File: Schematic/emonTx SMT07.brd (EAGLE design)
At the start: 100 x 80.3 mm, 115 parts, among them IC1 4066D, IC2 4066D, IC3 LMV324, J1 CON_HEADER_PRG_AVR_ICSP, Q2 DS18B20, U2 ATMEGA32U4, X10 BU-SMA-H, X2 CT2, X3 CT3, X4 STEREOJACK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

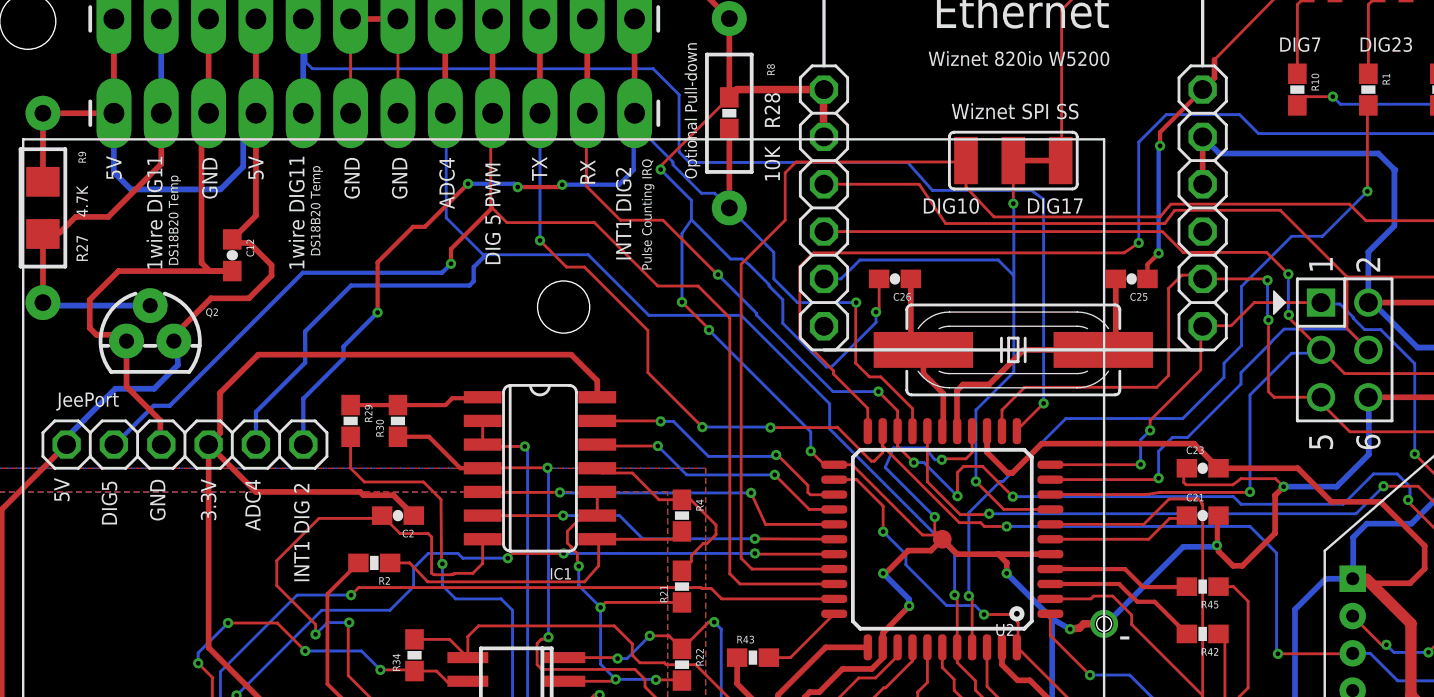
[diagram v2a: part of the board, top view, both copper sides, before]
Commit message: connect wiznet reset to dig5, need to route
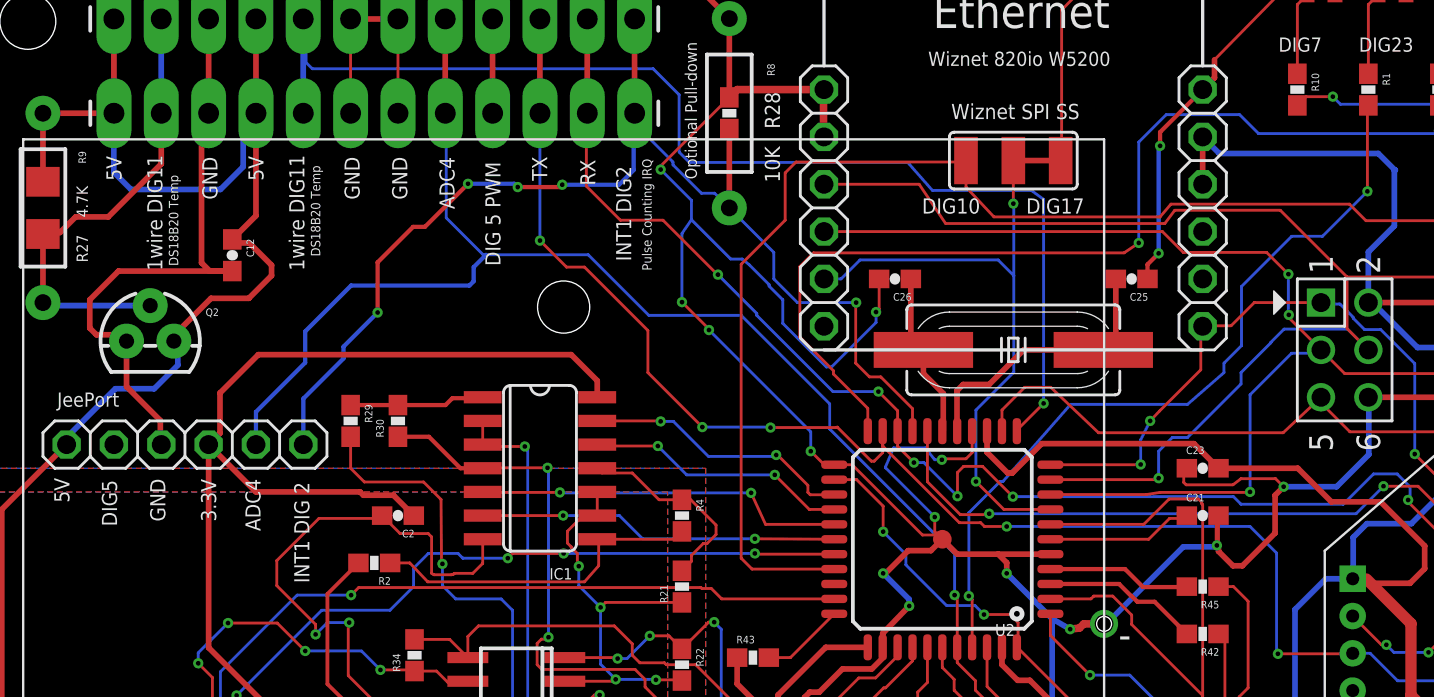
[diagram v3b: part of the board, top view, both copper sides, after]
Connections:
- net DIG5: now also JP3.5
- net RST: no longer JP3.5
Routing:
- net DIG5: track 71.0 -> 5.06 mm, vias 1 -> 0
- net RST: track 85.0 -> 75.3 mm, vias 2 -> 0
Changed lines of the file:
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@@
 <setting verticaltext="up"/>
 </settings>
-<grid distance="50" unitdist="mil" unit="mil" style="lines" multiple="1" display="yes" altdistance="50" altunitdist="mil" altunit="mil"/>
+<grid distance="5" unitdist="mil" unit="mil" style="lines" multiple="1" display="yes" altdistance="50" altunitdist="mil" altunit="mil"/>
 <layers>
 <layer number="1" name="Top" color="4" fill="1" visible="yes" active="yes"/>
@@
 <wire x1="55.27" y1="55.33" x2="55.27" y2="56.4638" width="0.1524" layer="1"/>
 <wire x1="55.27" y1="56.4638" x2="56.4896" y2="57.6834" width="0.1524" layer="1"/>
-<wire x1="56.4896" y1="57.6834" x2="63.5762" y2="57.6834" width="0.1524" layer="1"/>
-<wire x1="63.5762" y1="57.6834" x2="64.2112" y2="58.3184" width="0.1524" layer="1"/>
-<wire x1="64.2112" y1="58.3184" x2="64.2112" y2="62.992" width="0.1524" layer="1"/>
-<via x="69.5198" y="63.4238" extent="1-16" drill="0.25"/>
-<wire x1="69.5198" y1="63.4238" x2="69.5198" y2="61.341" width="0.1524" layer="16"/>
-<wire x1="69.5198" y1="61.341" x2="69.5706" y2="61.2902" width="0.1524" layer="16"/>
-<via x="69.5706" y="61.2902" extent="1-16" drill="0.25"/>
-<wire x1="69.5706" y1="61.2902" x2="69.5706" y2="57.4548" width="0.1524" layer="1"/>
-<wire x1="69.5706" y1="57.4548" x2="69.8754" y2="57.15" width="0.1524" layer="1"/>
-<wire x1="69.8754" y1="57.15" x2="72.39" y2="57.15" width="0.1524" layer="1"/>
 <wire x1="72.39" y1="57.15" x2="72.39" y2="56.8452" width="0.1524" layer="1"/>
 <wire x1="72.39" y1="56.8452" x2="73.9394" y2="55.2958" width="0.1524" layer="1"/>
@@
 <wire x1="97.116" y1="26.924" x2="97.4852" y2="26.924" width="0.1524" layer="1"/>
 <wire x1="97.4852" y1="26.924" x2="99.2886" y2="28.7274" width="0.1524" layer="1"/>
-<contactref element="JP3" pad="5"/>
-<wire x1="64.2112" y1="62.992" x2="64.9224" y2="63.7032" width="0.1524" layer="1"/>
-<wire x1="64.9224" y1="63.7032" x2="65.8368" y2="63.7032" width="0.1524" layer="1"/>
-<wire x1="65.8368" y1="63.7032" x2="66.04" y2="63.5" width="0.1524" layer="1"/>
-<wire x1="66.04" y1="63.5" x2="69.4436" y2="63.5" width="0.1524" layer="1"/>
-<wire x1="69.4436" y1="63.5" x2="69.5198" y2="63.4238" width="0.1524" layer="1"/>
+<wire x1="56.4896" y1="57.6834" x2="57.8866" y2="57.6834" width="0.1524" layer="1"/>
+<wire x1="57.8866" y1="57.6834" x2="60.452" y2="55.245" width="0.1524" layer="1"/>
+<wire x1="60.452" y1="55.245" x2="70.358" y2="55.245" width="0.1524" layer="1"/>
+<wire x1="70.358" y1="55.245" x2="72.39" y2="57.15" width="0.1524" layer="1"/>
 <wire x1="91.44" y1="7.112" x2="97.116" y2="26.924" width="0" layer="19" extent="1-1"/>
 </signal>
@@
 <via x="62.7126" y="53.5432" extent="1-16" drill="0.25"/>
 <wire x1="62.7126" y1="53.5432" x2="62.7126" y2="54.864" width="0.1524" layer="16"/>
-<wire x1="62.7126" y1="54.864" x2="63.2206" y2="55.372" width="0.1524" layer="16"/>
-<via x="63.2206" y="55.372" extent="1-16" drill="0.25"/>
-<wire x1="63.2206" y1="55.372" x2="63.2206" y2="55.9054" width="0.1524" layer="1"/>
-<wire x1="63.2206" y1="55.9054" x2="65.9384" y2="58.6232" width="0.1524" layer="1"/>
+<wire x1="62.7126" y1="54.864" x2="63.2206" y2="55.88" width="0.1524" layer="16"/>
+<via x="63.2206" y="55.88" extent="1-16" drill="0.25"/>
+<wire x1="63.2206" y1="55.88" x2="63.7286" y2="56.4134" width="0.1524" layer="1"/>
+<wire x1="63.7286" y1="56.4134" x2="65.9384" y2="58.6232" width="0.1524" layer="1"/>
 <wire x1="65.9384" y1="58.6232" x2="65.9384" y2="60.8584" width="0.1524" layer="1"/>
 <wire x1="65.9384" y1="60.8584" x2="66.04" y2="60.96" width="0.1524" layer="1"/>
@@
 <wire x1="53.4924" y1="50.9524" x2="55.1688" y2="52.6288" width="0.1524" layer="16"/>
 <wire x1="55.1688" y1="52.6288" x2="55.3212" y2="52.6288" width="0.1524" layer="16"/>
-<wire x1="55.3212" y1="52.6288" x2="58.6994" y2="56.007" width="0.1524" layer="16"/>
-<wire x1="58.6994" y1="56.007" x2="64.9732" y2="56.007" width="0.1524" layer="16"/>
-<wire x1="64.9732" y1="56.007" x2="67.183" y2="58.2168" width="0.1524" layer="16"/>
-<wire x1="67.183" y1="58.2168" x2="67.183" y2="58.9788" width="0.1524" layer="16"/>
+<wire x1="55.3212" y1="52.6288" x2="58.9534" y2="56.769" width="0.1524" layer="16"/>
+<wire x1="58.9534" y1="56.769" x2="65.2272" y2="56.769" width="0.1524" layer="16"/>
+<wire x1="65.2272" y1="56.769" x2="67.183" y2="58.4708" width="0.1524" layer="16"/>
+<wire x1="67.183" y1="58.4708" x2="67.183" y2="58.9788" width="0.1524" layer="16"/>
 <wire x1="67.183" y1="58.9788" x2="68.1228" y2="59.9186" width="0.1524" layer="16"/>
 <wire x1="68.1228" y1="59.9186" x2="68.1228" y2="63.0936" width="0.1524" layer="16"/>
@@
 <contactref element="JP5" pad="9"/>
 <contactref element="JP6" pad="2"/>
-<wire x1="46.27" y1="47.13" x2="41.2112" y2="47.13" width="0.1524" layer="1"/>
-<wire x1="41.2112" y1="47.13" x2="40.6654" y2="47.6758" width="0.1524" layer="1"/>
-<wire x1="40.6654" y1="47.6758" x2="40.6654" y2="61.4172" width="0.1524" layer="1"/>
-<wire x1="40.6654" y1="61.4172" x2="38.9636" y2="63.119" width="0.1524" layer="1"/>
-<wire x1="38.9636" y1="63.119" x2="36.8046" y2="63.119" width="0.1524" layer="1"/>
-<wire x1="36.8046" y1="63.119" x2="33.401" y2="66.5226" width="0.1524" layer="1"/>
-<wire x1="33.401" y1="66.5226" x2="28.702" y2="66.5226" width="0.1524" layer="1"/>
-<wire x1="28.702" y1="66.5226" x2="27.9146" y2="67.31" width="0.1524" layer="1"/>
-<wire x1="27.9146" y1="67.31" x2="27.8384" y2="67.3862" width="0.1524" layer="1"/>
-<wire x1="27.8384" y1="67.3862" x2="27.8384" y2="72.2884" width="0.1524" layer="1"/>
-<wire x1="27.8384" y1="72.2884" x2="27.94" y2="72.39" width="0.1524" layer="1"/>
-<wire x1="7.62" y1="54.61" x2="7.6708" y2="54.61" width="0.2286" layer="16"/>
-<wire x1="7.6708" y1="54.61" x2="9.7536" y2="56.6928" width="0.2286" layer="16"/>
-<wire x1="9.7536" y1="56.6928" x2="10.6172" y2="56.6928" width="0.2286" layer="16"/>
-<wire x1="10.6172" y1="56.6928" x2="17.7546" y2="63.8302" width="0.2286" layer="16"/>
-<wire x1="17.7546" y1="63.8302" x2="25.2222" y2="63.8302" width="0.2286" layer="16"/>
-<wire x1="25.2222" y1="63.8302" x2="25.7048" y2="64.3128" width="0.2286" layer="16"/>
-<via x="25.7048" y="64.3128" extent="1-16" drill="0.25"/>
-<wire x1="25.7048" y1="64.3128" x2="25.7048" y2="65.1002" width="0.2286" layer="1"/>
-<wire x1="25.7048" y1="65.1002" x2="27.9146" y2="67.31" width="0.2286" layer="1"/>
 <wire x1="27.9364375" y1="77.45100625" x2="27.9364375" y2="72.3935625" width="0.3048" layer="1"/>
 <wire x1="27.9364375" y1="72.3935625" x2="27.94" y2="72.39" width="0.3048" layer="1"/>
+<contactref element="JP3" pad="5"/>
+<wire x1="46.27" y1="47.13" x2="66.04" y2="63.5" width="0" layer="19" extent="1-1"/>
+<wire x1="27.94" y1="72.39" x2="46.27" y2="47.13" width="0" layer="19" extent="1-1"/>
+<wire x1="7.62" y1="54.61" x2="27.94" y2="72.39" width="0" layer="19" extent="1-1"/>
 </signal>
 <signal name="DIG7">
